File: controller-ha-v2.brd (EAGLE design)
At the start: 188 x 169.5 mm, 138 parts, among them U1 DS1307, U2 ARDUINO-MEGAPRO-5V, U3 ARDUINO-MEGAFULL

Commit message: Update to ver2
Added : Capacitors, DC/DC, DC input jack; Re-routed (fixed
too-close-through holes) + 9V DC and VCC clearence
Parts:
- removed U2: ARDUINO-MEGAPRO-5V, SparkFun-Boards:ARDUINO_MEGA-PRO-5V
- moved CN1 17.2 mm to (191.3, 17.8)
- moved ACDC 3.97 mm to (166.2, 41.8)
- moved U$1 2.95 mm to (132.2, 50.0)
- moved AC_IN 0.91 mm to (163.3, 3.24)
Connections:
- new net +9V: CN1.PWR, U$1.VIN
- net +3V3: no longer U$1.VOUT
- net VCC: now also U$1.VOUT; no longer CN1.PWR, U$1.VIN
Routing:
- net +9V: track 0.00 -> 55.0 mm
- net GND: track 1236.8 -> 1260.4 mm, vias 73 -> 83
- net DS_OE: track 367.1 -> 375.8 mm
- net VCC: track 1689.2 -> 1697.6 mm
- net SR_RST: track 331.8 -> 334.6 mm
- net SR_DS: track 302.3 -> 304.8 mm
- net STCP: track 364.0 -> 366.2 mm
- net N$17: track 25.9 -> 24.0 mm
- net SHCP: track 350.0 -> 351.8 mm
- net N$55: track 89.0 -> 88.0 mm
- net N$43: track 89.0 -> 88.0 mm
- net N$34: track 24.6 -> 24.1 mm
- net N$35: track 24.6 -> 24.1 mm
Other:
- board size 188 x 169.5 mm -> 189 x 169.5 mm

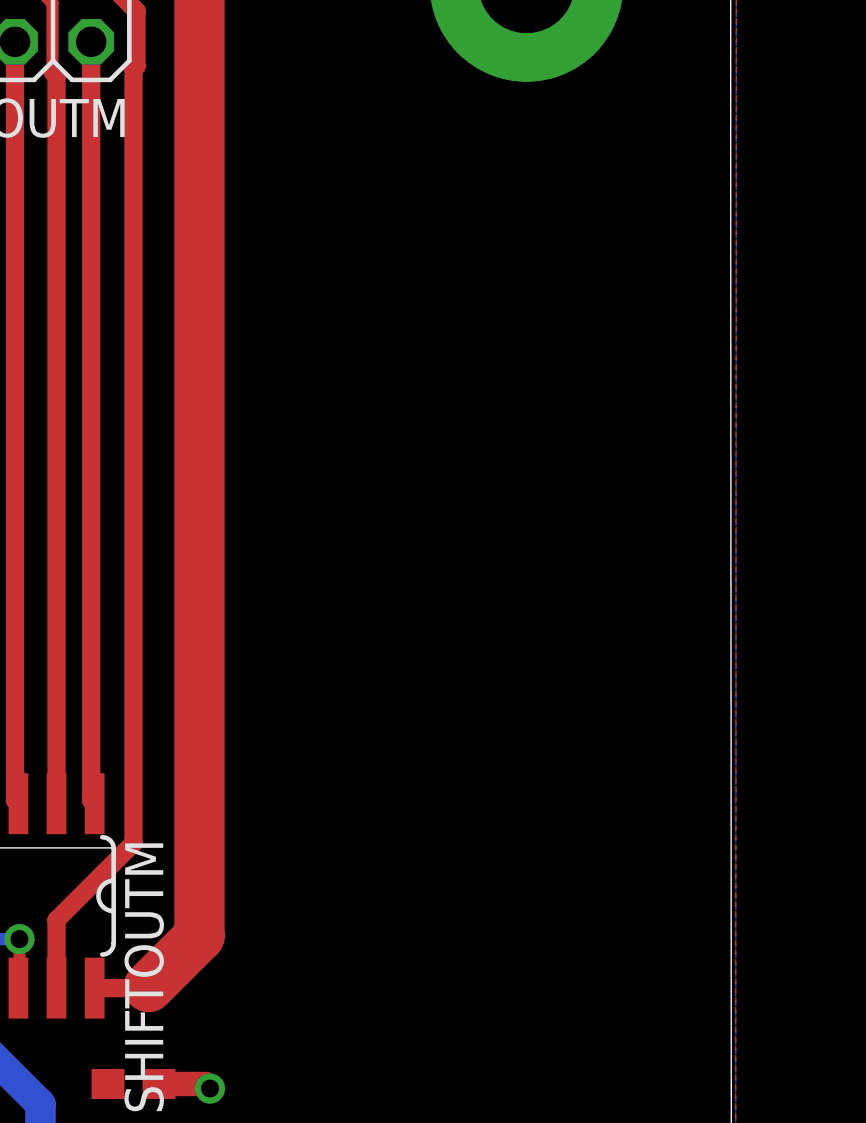
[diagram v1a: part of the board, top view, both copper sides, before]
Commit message: updated to ver3
Version 3 is separating the Main Controller and the I/O Module
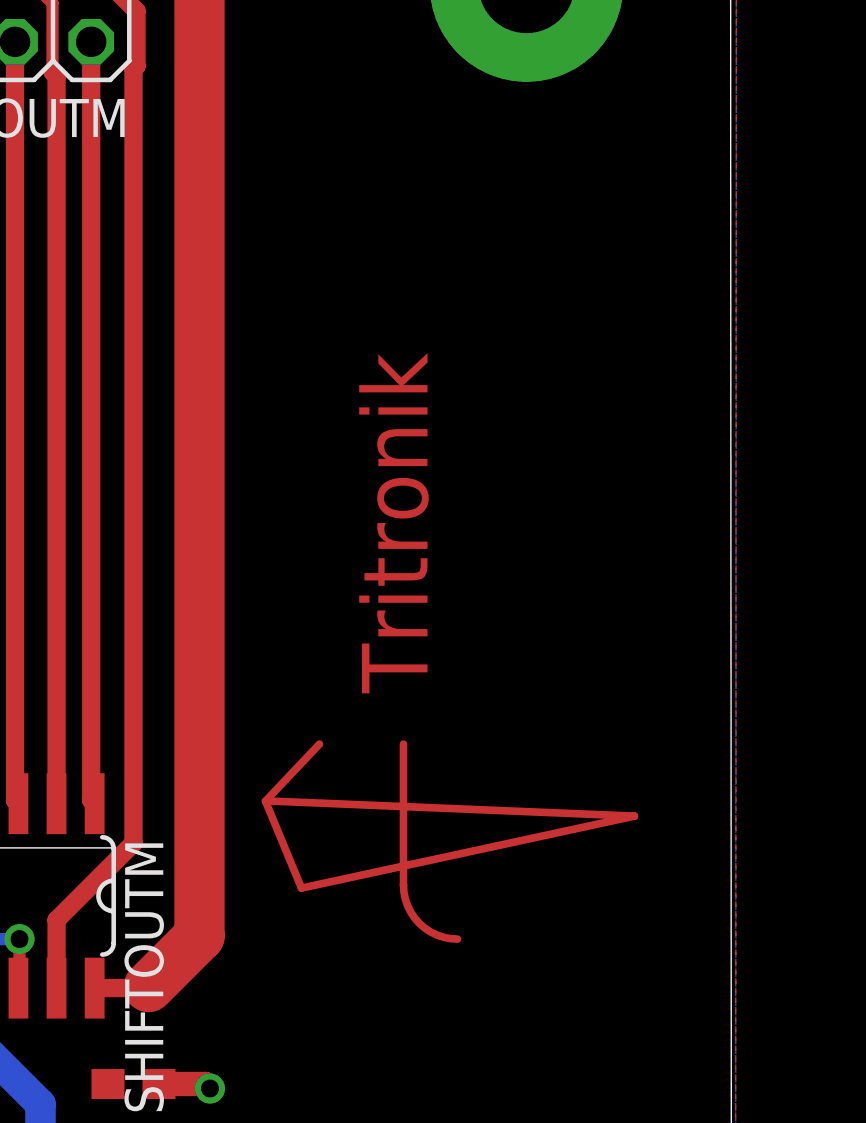
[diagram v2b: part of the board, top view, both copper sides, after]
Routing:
- net TRI: track 0.00 -> 36.5 mm
- added copper zone on layer 1, net TRI
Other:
- board text added: "Tritronik"
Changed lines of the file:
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@@
 <dimension x1="-0.1" y1="169.5" x2="187.8" y2="169.5" x3="93.85" y3="173" textsize="1.6764" layer="21"/>
 <dimension x1="0" y1="0" x2="-0.1" y2="169.5" x3="-5" y3="84.75" textsize="1.6764" layer="21" dtype="vertical"/>
+<text x="178.7" y="139.4" size="2.1844" layer="1" font="fixed" rot="R90">Tritronik</text>
 </plain>
 <attributes>
@@
 <contactref element="U$1" pad="VOUT"/>
 <wire x1="74.2" y1="102" x2="74.19" y2="101.99" width="0" layer="19" extent="16-16"/>
-<wire x1="121.6" y1="102.1" x2="121.57" y2="102.07" width="0" layer="19" extent="16-16"/>
 <wire x1="97.5" y1="102.1" x2="97.48" y2="102.12" width="0" layer="19" extent="16-16"/>
+<wire x1="121.6" y1="102.1" x2="121.57" y2="102.07" width="0" layer="19" extent="16-16"/>
 <wire x1="146.3" y1="102.3" x2="146.22" y2="102.28" width="0" layer="19" extent="16-16"/>
 </signal>
@@
 <wire x1="177.72" y1="37.88" x2="177.72" y2="17.79" width="1.6764" layer="1"/>
 </signal>
+<signal name="TRI">
+<wire x1="175.1" y1="137.7" x2="173.3" y2="135.8" width="0.254" layer="1"/>
+<wire x1="173.3" y1="135.8" x2="174.5" y2="132.9" width="0.254" layer="1"/>
+<wire x1="174.5" y1="132.9" x2="185.6" y2="135.3" width="0.254" layer="1"/>
+<wire x1="185.6" y1="135.3" x2="173.5" y2="135.8" width="0.254" layer="1"/>
+<polygon width="0.254" layer="1">
+<vertex x="173.3" y="135.8"/>
+<vertex x="174.5" y="132.9"/>
+<vertex x="185.6" y="135.3"/>
+</polygon>
+<wire x1="179.7" y1="131.2" x2="177.9" y2="133" width="0.254" layer="1" curve="-90"/>
+<wire x1="177.9" y1="133" x2="177.9" y2="137.7" width="0.254" layer="1"/>
+<wire x1="175.1" y1="137.7" x2="177.9" y2="137.7" width="0" layer="19" extent="1-1"/>
+</signal>
 </signals>
